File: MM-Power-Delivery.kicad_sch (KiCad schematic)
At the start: 5 parts, among them J7 JST Connector, J8 JST Connector, U8 Voltage Regulator

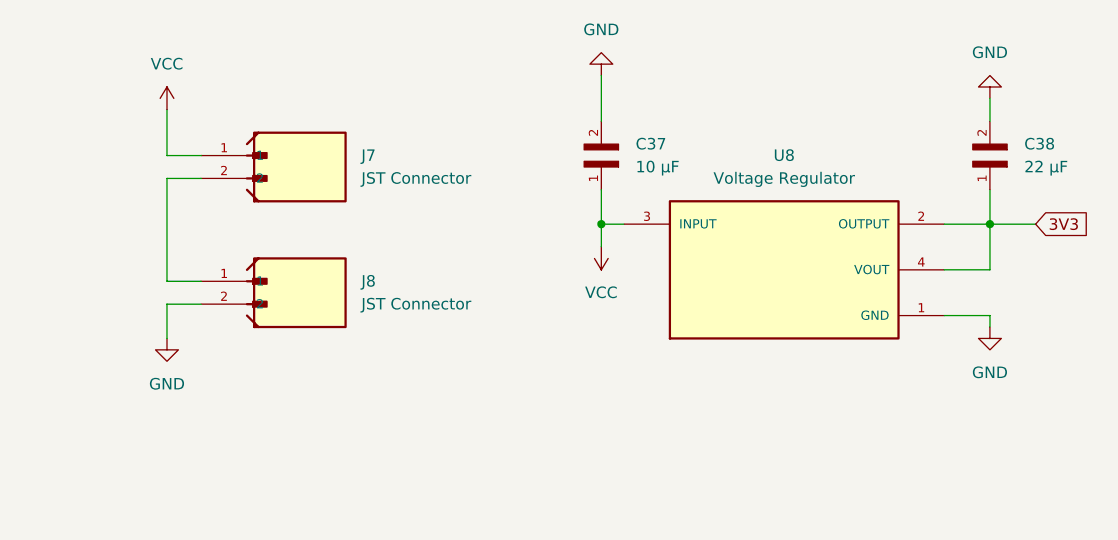
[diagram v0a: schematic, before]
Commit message: added power switch
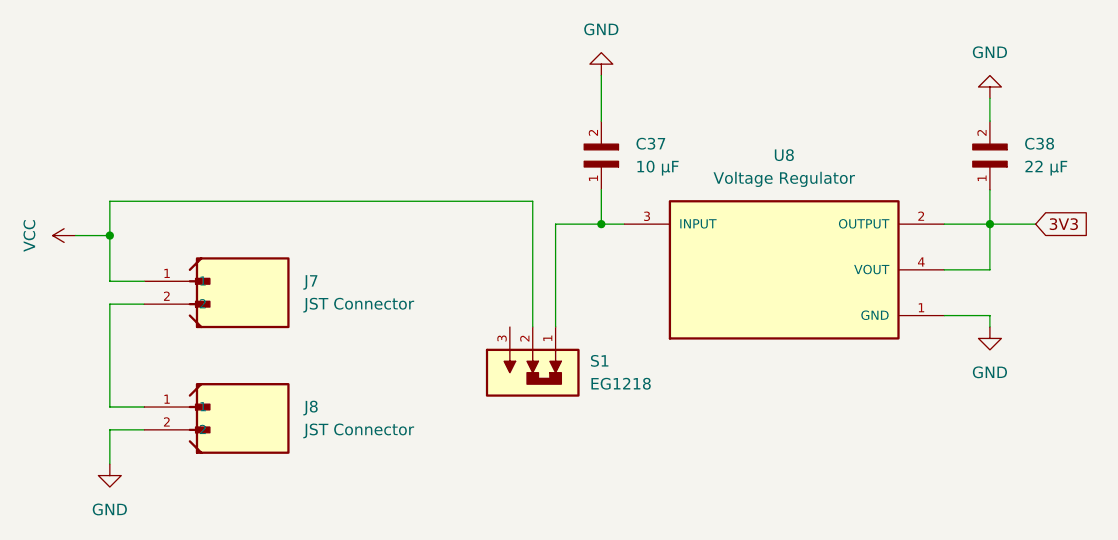
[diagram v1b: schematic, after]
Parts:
- added S1: EG1218, EG1218:SW_EG1218, symbol Slide_Switch_EG1218:EG1218
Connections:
- net VCC: now also S1.2; no longer C37.1, U8.3 (INPUT)
- new net: C37.1, S1.1, U8.3 (INPUT)
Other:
- moved on the sheet: J7, J8

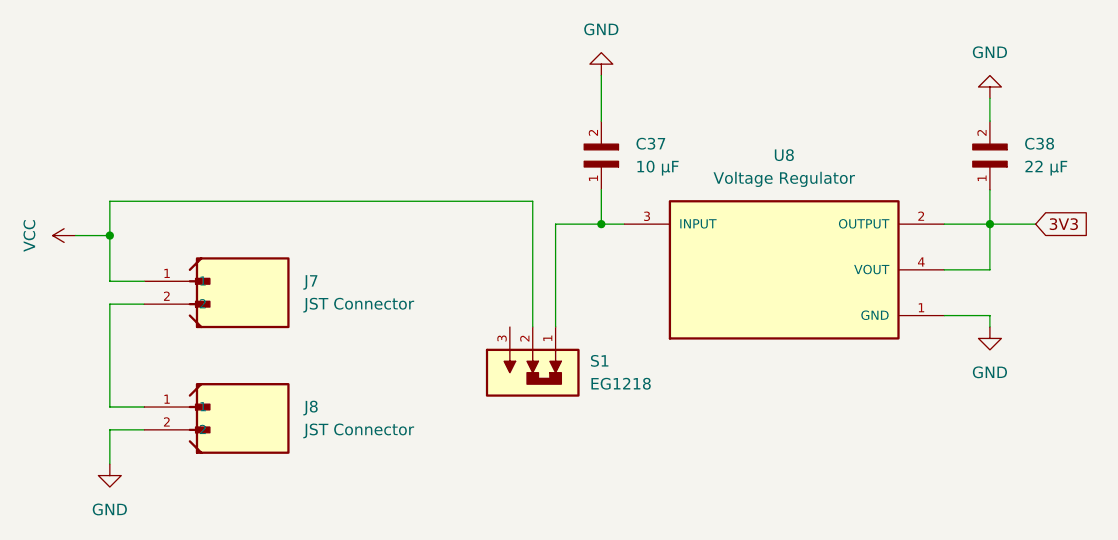
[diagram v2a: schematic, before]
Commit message: redid the 4 emitters receivers, fixed orientation of LEDS and going to continue adding footprints and replace the 60ohm resistors with 300ohm ones
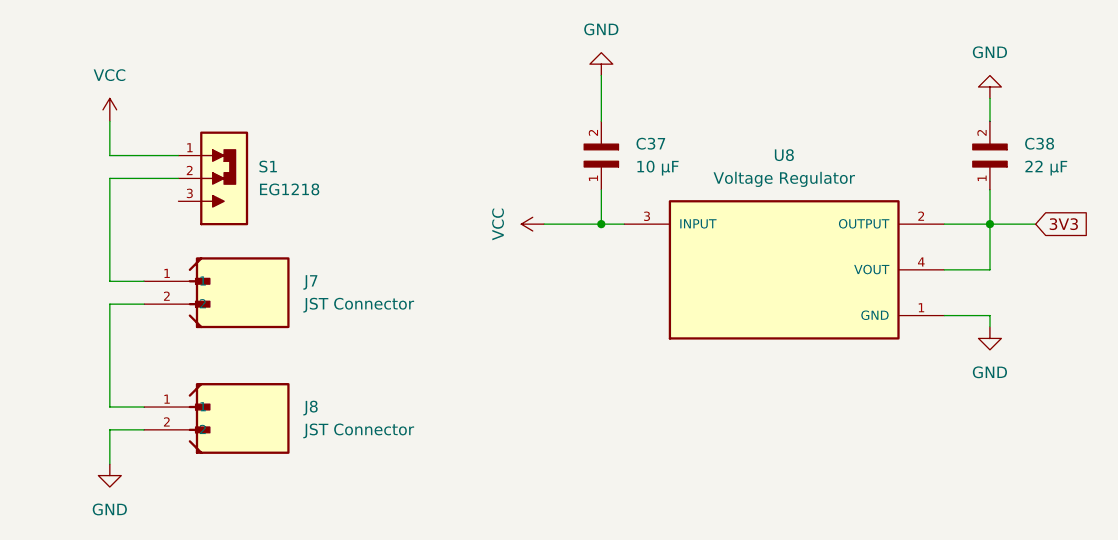
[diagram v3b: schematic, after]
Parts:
- C37: footprint CL21B106KOQNNNE:CAPC2012X140N -> Ceramic_Capacitor_10uF_GRM21BC81C106KA73L:CAPC2012X140N
- C38: footprint CL21A226MPQNNNE:CAPC2012X140N -> Ceramic_Capacitor_22uF_CL21A226KPCLRNC:CAPC2012X95N
- J7, J8: footprint B2B_PH_K_S:JST_B2B-PH-K-S -> JST_Connector_B2B-PH-K-S:JST_B2B-PH-K-S
- S1: footprint EG1218:SW_EG1218 -> Slide_Switch_EG1218:SW_EG1218
- U8: footprint AZ1117IH-3.3TRG1:SOT230P700X185-4N -> Voltage_Regulator_AZ1117IH-3.3TRG1:SOT230P700X185-4N
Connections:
- net VCC: now also C37.1, S1.1, U8.3 (INPUT); no longer J7.1, S1.2
- new net: J7.1, S1.2
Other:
- moved on the sheet: S1
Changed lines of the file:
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@@
 	(paper "A4")
-	(junction
-		(at 74.93 92.71)
-		(diameter 0)
-		(color 0 0 0 0)
-	)
 	(junction
 		(at 129.54 91.44)
@@
 	(wire
 		(pts
-			(xy 124.46 91.44) (xy 129.54 91.44)
-		)
-		(stroke
-			(width 0)
-			(type default)
-		)
-	)
-	(wire
-		(pts
-			(xy 74.93 88.9) (xy 74.93 92.71)
+			(xy 123.19 91.44) (xy 129.54 91.44)
 		)
 		(stroke
@@
 	(wire
 		(pts
+			(xy 74.93 83.82) (xy 82.55 83.82)
+		)
+		(stroke
+			(width 0)
+			(type default)
+		)
+	)
+	(wire
+		(pts
+			(xy 74.93 80.01) (xy 74.93 83.82)
+		)
+		(stroke
+			(width 0)
+			(type default)
+		)
+	)
+	(wire
+		(pts
 			(xy 132.08 91.44) (xy 129.54 91.44)
 		)
@@
 	(wire
 		(pts
-			(xy 74.93 92.71) (xy 74.93 97.79)
-		)
-		(stroke
-			(width 0)
-			(type default)
-		)
-	)
-	(wire
-		(pts
-			(xy 74.93 88.9) (xy 121.92 88.9)
+			(xy 74.93 86.36) (xy 74.93 97.79)
 		)
 		(stroke
@@
 	(wire
 		(pts
-			(xy 124.46 91.44) (xy 124.46 102.87)
-		)
-		(stroke
-			(width 0)
-			(type default)
-		)
-	)
-	(wire
-		(pts
 			(xy 167.64 91.44) (xy 172.72 91.44)
 		)
@@
 	(wire
 		(pts
-			(xy 121.92 88.9) (xy 121.92 102.87)
-		)
-		(stroke
-			(width 0)
-			(type default)
-		)
-	)
-	(wire
-		(pts
-			(xy 71.12 92.71) (xy 74.93 92.71)
-		)
-		(stroke
-			(width 0)
-			(type default)
-		)
-	)
-	(wire
-		(pts
 			(xy 129.54 74.93) (xy 129.54 80.01)
 		)
@@
 		(pts
 			(xy 172.72 96.52) (xy 167.64 96.52)
+		)
+		(stroke
+			(width 0)
+			(type default)
+		)
+	)
+	(wire
+		(pts
+			(xy 74.93 86.36) (xy 82.55 86.36)
 		)
 		(stroke
@@
 			)
 		)
-		(property "Footprint" "B2B_PH_K_S:JST_B2B-PH-K-S"
+		(property "Footprint" "JST_Connector_B2B-PH-K-S:JST_B2B-PH-K-S"
 			(at 88.9 114.3 0)
 			(effects
@@
 			)
 		)
-		(property "Footprint" "CL21B106KOQNNNE:CAPC2012X140N"
+		(property "Footprint" "Ceramic_Capacitor_10uF_GRM21BC81C106KA73L:CAPC2012X140N"
 			(at 129.54 85.09 0)
 			(effects
@@
 			)
 		)
-		(property "Footprint" "AZ1117IH-3.3TRG1:SOT230P700X185-4N"
+		(property "Footprint" "Voltage_Regulator_AZ1117IH-3.3TRG1:SOT230P700X185-4N"
 			(at 149.86 96.52 0)
 			(effects
@@
 	(symbol
 		(lib_id "Slide_Switch_EG1218:EG1218")
-		(at 121.92 107.95 270)
+		(at 87.63 86.36 0)
 		(unit 1)
 		(exclude_from_sim no)
@@
 		(fields_autoplaced yes)
 		(property "Reference" "S1"
-			(at 128.27 106.6799 90)
+			(at 91.44 85.0899 0)
 			(effects
 				(font
@@
 		)
 		(property "Value" "EG1218"
-			(at 128.27 109.2199 90)
+			(at 91.44 87.6299 0)
 			(effects
 				(font
@@
 			)
 		)
-		(property "Footprint" "EG1218:SW_EG1218"
-			(at 121.92 107.95 0)
+		(property "Footprint" "Slide_Switch_EG1218:SW_EG1218"
+			(at 87.63 86.36 0)
 			(effects
 				(font
@@
 		)
 		(property "Datasheet" ""
-			(at 121.92 107.95 0)
+			(at 87.63 86.36 0)
 			(effects
 				(font
@@
 		)
 		(property "Description" ""
-			(at 121.92 107.95 0)
+			(at 87.63 86.36 0)
 			(effects
 				(font
@@
 		)
 		(property "DigiKey_Part_Number" "EG1903-ND"
-			(at 121.92 107.95 0)
+			(at 87.63 86.36 0)
 			(effects
 				(font
@@
 		)
 		(property "MF" "E-Switch"
-			(at 121.92 107.95 0)
+			(at 87.63 86.36 0)
 			(effects
 				(font
@@
 		)
 		(property "DESCRIPTION" "Slide Switch SPDT Through Hole"
-			(at 121.92 107.95 0)
+			(at 87.63 86.36 0)
 			(effects
 				(font
@@
 		)
 		(property "PACKAGE" "None"
-			(at 121.92 107.95 0)
+			(at 87.63 86.36 0)
 			(effects
 				(font
@@
 		)
 		(property "PRICE" "None"
-			(at 121.92 107.95 0)
+			(at 87.63 86.36 0)
 			(effects
 				(font
@@
 		)
 		(property "Package" "None"
-			(at 121.92 107.95 0)
+			(at 87.63 86.36 0)
 			(effects
 				(font
@@
 		)
 		(property "Check_prices" "https://www.snapeda.com/parts/EG1218/E-Switch/view-part/?ref=eda"
-			(at 121.92 107.95 0)
+			(at 87.63 86.36 0)
 			(effects
 				(font
@@
 		)
 		(property "SnapEDA_Link" "https://www.snapeda.com/parts/EG1218/E-Switch/view-part/?ref=snap"
-			(at 121.92 107.95 0)
+			(at 87.63 86.36 0)
 			(effects
 				(font
@@
 		)
 		(property "MP" "EG1218"
-			(at 121.92 107.95 0)
+			(at 87.63 86.36 0)
 			(effects
 				(font
@@
 		)
 		(property "Description_1" "Slide Switch, EG Series, SPDT, Non-Shorting, ON-ON, 200mA DC, 30VDC, PC Pin | E-Switch EG1218"
-			(at 121.92 107.95 0)
+			(at 87.63 86.36 0)
 			(effects
 				(font
@@
 		)
 		(property "AVAILABILITY" "In Stock"
-			(at 121.92 107.95 0)
+			(at 87.63 86.36 0)
 			(effects
 				(font
@@
 		)
 		(property "PURCHASE-URL" "https://pricing.snapeda.com/search/part/EG1218/?ref=eda"
-			(at 121.92 107.95 0)
+			(at 87.63 86.36 0)
 			(effects
 				(font
@@
 	(symbol
 		(lib_id "power:VCC")
-		(at 71.12 92.71 90)
+		(at 123.19 91.44 90)
+		(unit 1)
+		(exclude_from_sim no)
+		(in_bom yes)
+		(on_board yes)
+		(dnp no)
+		(property "Reference" "#PWR01"
+			(at 127 91.44 0)
+			(effects
+				(font
+					(size 1.27 1.27)
+				)
+				(hide yes)
+			)
+		)
+		(property "Value" "VCC"
+			(at 118.11 91.44 0)
+			(effects
+				(font
+					(size 1.27 1.27)
+				)
+			)
+		)
+		(property "Footprint" ""
+			(at 123.19 91.44 0)
+			(effects
+				(font
+					(size 1.27 1.27)
+				)
+				(hide yes)
+			)
+		)
+		(property "Datasheet" ""
+			(at 123.19 91.44 0)
+			(effects
+				(font
+					(size 1.27 1.27)
+				)
+				(hide yes)
+			)
+		)
+		(property "Description" "Power symbol creates a global label with name \"VCC\""
+			(at 123.19 91.44 0)
+			(effects
+				(font
+					(size 1.27 1.27)
+				)
+				(hide yes)
+			)
+		)
+		(pin "1"
+		)
+		(instances
+			(project "IREmitter"
+				(path "/d311851a-8b0b-4acf-b2e7-1b968b2adbe7/0b36aac1-160e-4635-9375-c6b7de12d273"
+					(reference "#PWR01")
+					(unit 1)
+				)
+			)
+		)
+	)
+	(symbol
+		(lib_id "power:VCC")
+		(at 74.93 80.01 0)
 		(unit 1)
 		(exclude_from_sim no)
@@
 		(dnp no)
 		(property "Reference" "#PWR012"
-			(at 74.93 92.71 0)
+			(at 74.93 83.82 0)
 			(effects
 				(font
@@
 		)
 		(property "Value" "VCC"
-			(at 66.04 92.71 0)
+			(at 74.93 74.93 0)
 			(effects
 				(font
@@
 		)
 		(property "Footprint" ""
-			(at 71.12 92.71 0)
+			(at 74.93 80.01 0)
 			(effects
 				(font
@@
 		)
 		(property "Datasheet" ""
-			(at 71.12 92.71 0)
+			(at 74.93 80.01 0)
 			(effects
 				(font
@@
 		)
 		(property "Description" "Power symbol creates a global label with name \"VCC\""
-			(at 71.12 92.71 0)
+			(at 74.93 80.01 0)
 			(effects
 				(font
@@
 			)
 		)
-		(property "Footprint" "B2B_PH_K_S:JST_B2B-PH-K-S"
+		(property "Footprint" "JST_Connector_B2B-PH-K-S:JST_B2B-PH-K-S"
 			(at 88.9 100.33 0)
 			(effects
@@
 			)
 		)
-		(property "Footprint" "CL21A226MPQNNNE:CAPC2012X140N"
+		(property "Footprint" "Ceramic_Capacitor_22uF_CL21A226KPCLRNC:CAPC2012X95N"
 			(at 172.72 85.09 0)
 			(effects

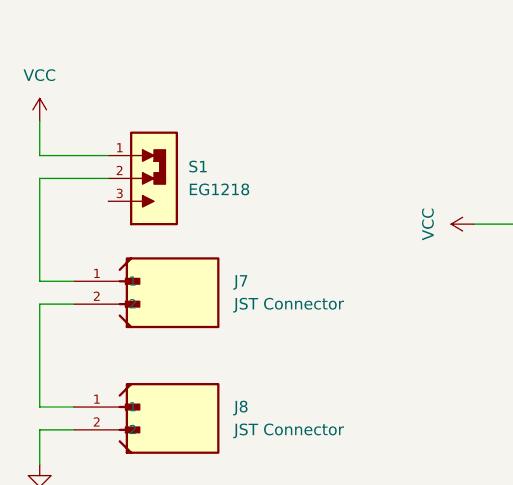
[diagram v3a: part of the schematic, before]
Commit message: LED changes, mosfet footprint fixed
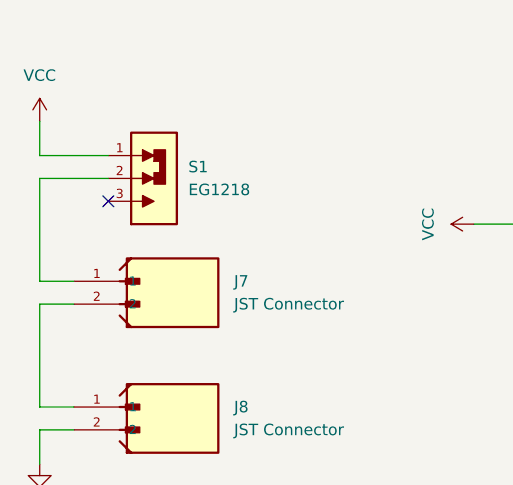
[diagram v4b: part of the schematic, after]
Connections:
- no-connect marks 0 -> 1
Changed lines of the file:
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@@
 		(color 0 0 0 0)
+	)
+	(no_connect
+		(at 82.55 88.9)
 	)
 	(wire

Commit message: finished edits on PCB - hopefully final
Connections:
- net GND: no longer J8.2
- new net MGND: J8.2
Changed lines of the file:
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@@
+	(symbol
+		(lib_id "power:GND")
+		(at 74.93 118.11 0)
+		(unit 1)
+		(exclude_from_sim no)
+		(in_bom yes)
+		(on_board yes)
+		(dnp no)
+		(fields_autoplaced yes)
+		(property "Reference" "#PWR05"
+			(at 74.93 124.46 0)
+			(effects
+				(font
+					(size 1.27 1.27)
+				)
+				(hide yes)
+			)
+		)
+		(property "Value" "MGND"
+			(at 74.93 123.19 0)
+			(effects
+				(font
+					(size 1.27 1.27)
+				)
+			)
+		)
+		(property "Footprint" ""
+			(at 74.93 118.11 0)
+			(effects
+				(font
+					(size 1.27 1.27)
+				)
+				(hide yes)
+			)
+		)
+		(property "Datasheet" ""
+			(at 74.93 118.11 0)
+			(effects
+				(font
+					(size 1.27 1.27)
+				)
+				(hide yes)
+			)
+		)
+		(property "Description" "Power symbol creates a global label with name \"GND\" , ground"
+			(at 74.93 118.11 0)
+			(effects
+				(font
+					(size 1.27 1.27)
+				)
+				(hide yes)
+			)
+		)
+		(pin "1"
+		)
+		(instances
+			(project ""
+				(path "/d311851a-8b0b-4acf-b2e7-1b968b2adbe7/0b36aac1-160e-4635-9375-c6b7de12d273"
+					(reference "#PWR05")
+					(unit 1)
+				)
+			)
+		)
+	)
 	(symbol
 		(lib_id "power:GND")
@@
 					(unit 1)
 				)
-			)
-		)
-	)
-	(symbol
-		(lib_id "power:GND")
-		(at 74.93 118.11 0)
-		(unit 1)
-		(exclude_from_sim no)
-		(in_bom yes)
-		(on_board yes)
-		(dnp no)
-		(fields_autoplaced yes)
-		(property "Reference" "#PWR013"
-			(at 74.93 124.46 0)
-			(effects
-				(font
-					(size 1.27 1.27)
-				)
-				(hide yes)
-			)
-		)
-		(property "Value" "GND"
-			(at 74.93 123.19 0)
-			(effects
-				(font
-					(size 1.27 1.27)
-				)
-			)
-		)
-		(property "Footprint" ""
-			(at 74.93 118.11 0)
-			(effects
-				(font
-					(size 1.27 1.27)
-				)
-				(hide yes)
-			)
-		)
-		(property "Datasheet" ""
-			(at 74.93 118.11 0)
-			(effects
-				(font
-					(size 1.27 1.27)
-				)
-				(hide yes)
-			)
-		)
-		(property "Description" "Power symbol creates a global label with name \"GND\" , ground"
-			(at 74.93 118.11 0)
-			(effects
-				(font
-					(size 1.27 1.27)
-				)
-				(hide yes)
-			)
-		)
-		(pin "1"
-		)
-		(instances
-			(project "IREmitter"
-				(path "/d311851a-8b0b-4acf-b2e7-1b968b2adbe7/0b36aac1-160e-4635-9375-c6b7de12d273"
-					(reference "#PWR013")
-					(unit 1)
-				)
